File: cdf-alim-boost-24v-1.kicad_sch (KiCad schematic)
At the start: 0 parts

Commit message: schem: add batt input
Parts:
- added C2: 1u, Capacitor_SMD:C_0402_1005Metric, symbol Device:C
- added C3: 1n, Capacitor_SMD:C_0402_1005Metric, symbol Device:C
- added C7, C9: 10u, Capacitor_SMD:C_0805_2012Metric, symbol Device:C
- added D2: SMBJ6.0CA, Diode_SMD:D_SMA, symbol Device:D_TVS
- added D4: GREEN, LED_SMD:LED_0805_2012Metric, symbol Device:LED
- added J2: Conn_01x02, Connector_JST:JST_XH_S2B-XH-A-1_1x02_P2.50mm_Horizontal, symbol Connector_Generic:Conn_01x02
- added JP1: Jumper_2_Small_Bridged, Connector_PinHeader_2.54mm:PinHeader_1x02_P2.54mm_Vertical, symbol Jumper:Jumper_2_Small_Bridged
- added R11: 5k1, Resistor_SMD:R_0402_1005Metric, symbol Device:R
- added R5: 10k, Resistor_SMD:R_0402_1005Metric, symbol Device:R
- added R6: 1k, Resistor_SMD:R_0402_1005Metric, symbol Device:R
- added R7: 3k3, Resistor_SMD:R_0402_1005Metric, symbol Device:R
- added TP2: TestPoint, TestPoint:TestPoint_Pad_D2.0mm, symbol Connector:TestPoint
- added U1: TPS259470x, GLCS:Texas_RPW0010A_VQFN-HR-10_2x2mm_P0.5mm, symbol GLCS:TPS259470x
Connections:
- new net: C3.1, U1.7 (DVDT)
- new net: C2.2, D2.1 (A1), J2.2 (Pin_2), R5.2, U1.5 (IN)
- new net: D4.1 (K), U1.4 (~{FLT})
- new net: D4.2 (A), R11.1
- new net: JP1.1 (A), U1.6 (OUT)
- new net: C7.1, C9.1, JP1.2 (B)
- new net +3V3: R11.2
- new net BATT1_V: R5.1, R6.2, U1.1 (EN/UVLO)
- new net GND: C2.1, C3.2, C7.2, C9.2, D2.2 (A2), J2.1 (Pin_1), R6.1, R7.2, U1.2 (OVLO), U1.8 (GND)
- new net ILM1: R7.1, TP2.1, U1.9 (ILM)
- no-connect marks 0 -> 2
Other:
- note added: "UVLO = 13.2V Slew Rate 250mA limit for 100uF load -> 2.5V/ms -> Cdvdt = 800pF (BOM consolidation) For 1n -> SR ~ 2V/ms Ilim ->Ilim = 1A ->I = Vilm(µV)/(180*3300)"

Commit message: schem: remove efuse
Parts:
- removed C2: 1u, Capacitor_SMD:C_0402_1005Metric, symbol Device:C
- removed C3: 1n, Capacitor_SMD:C_0402_1005Metric, symbol Device:C
- removed C7, C9: 10u, Capacitor_SMD:C_0805_2012Metric, symbol Device:C
- removed D4: GREEN, LED_SMD:LED_0805_2012Metric, symbol Device:LED
- removed JP1: Jumper_2_Small_Bridged, Connector_PinHeader_2.54mm:PinHeader_1x02_P2.54mm_Vertical, symbol Jumper:Jumper_2_Small_Bridged
- removed R11: 5k1, Resistor_SMD:R_0402_1005Metric, symbol Device:R
- removed R5: 10k, Resistor_SMD:R_0402_1005Metric, symbol Device:R
- removed R6: 1k, Resistor_SMD:R_0402_1005Metric, symbol Device:R
- removed R7: 3k3, Resistor_SMD:R_0402_1005Metric, symbol Device:R
- removed TP2: TestPoint, TestPoint:TestPoint_Pad_D2.0mm, symbol Connector:TestPoint
- removed U1: TPS259470x, GLCS:Texas_RPW0010A_VQFN-HR-10_2x2mm_P0.5mm, symbol GLCS:TPS259470x
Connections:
- no-connect marks 2 -> 0
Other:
- note removed: "UVLO = 13.2V Slew Rate 250mA limit for 100uF load -> 2.5V/ms -> Cdvdt = 800pF (BOM consolidation) For 1n -> SR ~ 2V/ms Ilim ->Ilim = 1A ->I = Vilm(µV)/(180*3300)"
- moved on the sheet: D2

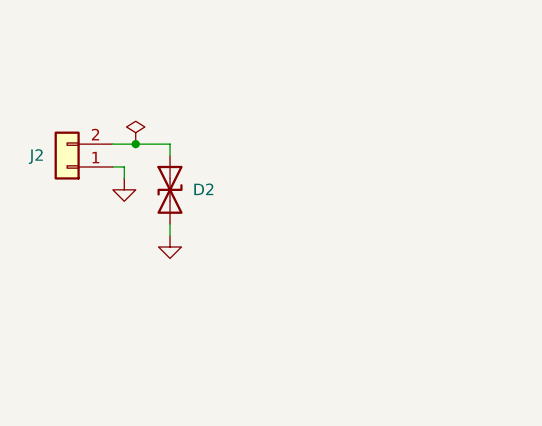
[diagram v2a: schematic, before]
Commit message: schem: add mosfet
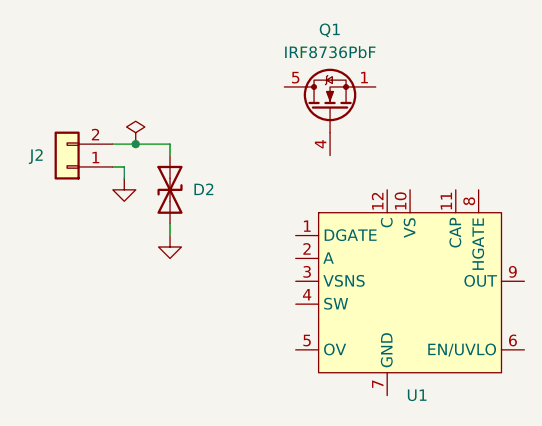
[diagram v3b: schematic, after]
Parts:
- added Q1: IRF8736PbF, Package_SO:SOIC-8_3.9x4.9mm_P1.27mm, symbol Transistor_FET:IRF8721PBF-1
- added U1: (no value), GLCS:WSON-12-1EP_3x3mm_P0.5mm_EP1.3x2.5mm_ThermalVias, symbol GLCS:LM74800
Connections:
- new net: Q1.1 (S), Q1.2 (S), Q1.3 (S)
- new net: Q1.5 (D), Q1.6 (D), Q1.7 (D), Q1.8 (D)
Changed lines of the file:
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@@
+	)
+	(symbol
+		(lib_id "Transistor_FET:IRF8721PBF-1")
+		(at 55.88 22.86 90)
+		(unit 1)
+		(body_style 1)
+		(exclude_from_sim no)
+		(in_bom yes)
+		(on_board yes)
+		(in_pos_files yes)
+		(dnp no)
+		(fields_autoplaced yes)
+		(property "Reference" "Q1"
+			(at 55.88 13.97 90)
+			(show_name no)
+			(do_not_autoplace no)
+			(effects
+				(font
+					(size 1.27 1.27)
+				)
+			)
+		)
+		(property "Value" "IRF8736PbF"
+			(at 55.88 16.51 90)
+			(show_name no)
+			(do_not_autoplace no)
+			(effects
+				(font
+					(size 1.27 1.27)
+				)
+			)
+		)
+		(property "Footprint" "Package_SO:SOIC-8_3.9x4.9mm_P1.27mm"
+			(at 57.785 17.78 0)
+			(hide yes)
+			(show_name no)
+			(do_not_autoplace no)
+			(effects
+				(font
+					(size 1.27 1.27)
+					(italic yes)
+				)
+				(justify left)
+			)
+		)
+		(property "Datasheet" "http://www.irf.com/product-info/datasheets/data/irf8721pbf-1.pdf"
+			(at 59.69 17.78 0)
+			(hide yes)
+			(show_name no)
+			(do_not_autoplace no)
+			(effects
+				(font
+					(size 1.27 1.27)
+				)
+				(justify left)
+			)
+		)
+		(property "Description" "14A Id, 30V Vds, HEXFET N-Channel MOSFET, SO-8"
+			(at 55.88 22.86 0)
+			(hide yes)
+			(show_name no)
+			(do_not_autoplace no)
+			(effects
+				(font
+					(size 1.27 1.27)
+				)
+			)
+		)
+		(pin "8"
+		)
+		(pin "2"
+		)
+		(pin "4"
+		)
+		(pin "7"
+		)
+		(pin "1"
+		)
+		(pin "5"
+		)
+		(pin "3"
+		)
+		(pin "6"
+		)
+		(instances
+			(project "cdf-alim-boost-24v-1"
+				(path "/c1d68e1e-31aa-4338-bfd5-3714fe43b2c6"
+					(reference "Q1")
+					(unit 1)
+				)
+			)
+		)
 	)
 	(symbol
@@
 					(unit 1)
 				)
+			)
+		)
+	)
+	(symbol
+		(lib_id "GLCS:LM74800")
+		(at 62.23 43.18 0)
+		(unit 1)
+		(body_style 1)
+		(exclude_from_sim no)
+		(in_bom yes)
+		(on_board yes)
+		(in_pos_files yes)
+		(dnp no)
+		(fields_autoplaced yes)
+		(property "Reference" "U1"
+			(at 64.3733 54.61 0)
+			(show_name no)
+			(do_not_autoplace no)
+			(effects
+				(font
+					(size 1.27 1.27)
+				)
+				(justify left)
+			)
+		)
+		(property "Value" ""
+			(at 62.23 43.18 0)
+			(show_name no)
+			(do_not_autoplace no)
+			(effects
+				(font
+					(size 1.27 1.27)
+				)
+			)
+		)
+		(property "Footprint" "GLCS:WSON-12-1EP_3x3mm_P0.5mm_EP1.3x2.5mm_ThermalVias"
+			(at 62.23 43.18 0)
+			(hide yes)
+			(show_name no)
+			(do_not_autoplace no)
+			(effects
+				(font
+					(size 1.27 1.27)
+				)
+			)
+		)
+		(property "Datasheet" ""
+			(at 62.23 43.18 0)
+			(hide yes)
+			(show_name no)
+			(do_not_autoplace no)
+			(effects
+				(font
+					(size 1.27 1.27)
+				)
+			)
+		)
+		(property "Description" ""
+			(at 62.23 43.18 0)
+			(hide yes)
+			(show_name no)
+			(do_not_autoplace no)
+			(effects
+				(font
+					(size 1.27 1.27)
+				)
+			)
+		)
+		(pin "9"
+		)
+		(pin "11"
+		)
+		(pin "7"
+		)
+		(pin "2"
+		)
+		(pin "1"
+		)
+		(pin "10"
+		)
+		(pin "4"
+		)
+		(pin "12"
+		)
+		(pin "8"
+		)
+		(pin "3"
+		)
+		(pin "RTN"
+		)
+		(pin "6"
+		)
+		(pin "5"
+		)
+		(instances
+			(project "cdf-alim-boost-24v-1"
+				(path "/c1d68e1e-31aa-4338-bfd5-3714fe43b2c6"
+					(reference "U1")
+					(unit 1)
+				)

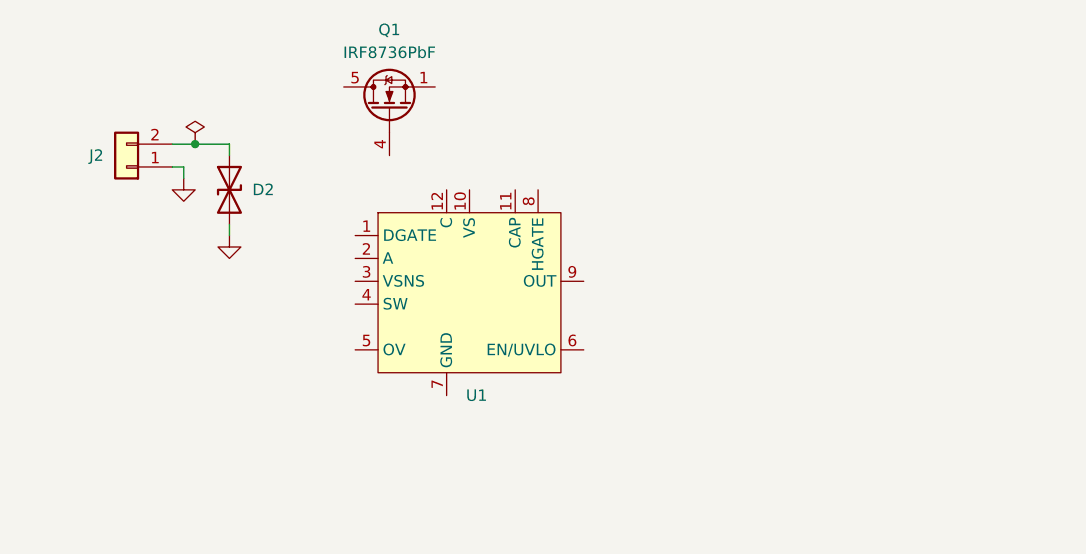
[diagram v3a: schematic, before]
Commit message: schem: initial ideal diode
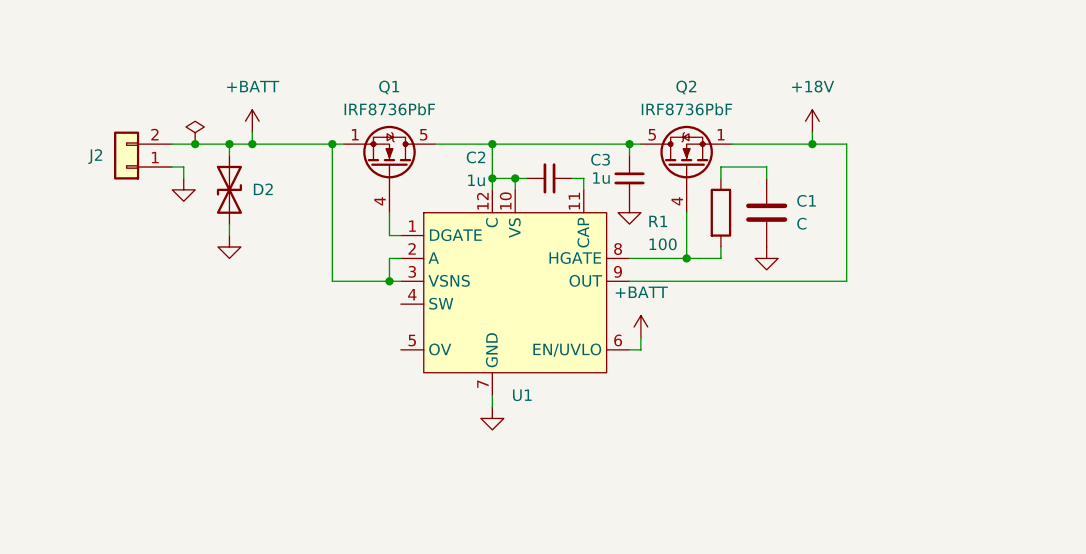
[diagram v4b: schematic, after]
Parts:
- added C1: C, symbol Device:C
- added C2, C3: 1u, Capacitor_SMD:C_0402_1005Metric, symbol Device:C_Small
- added Q2: IRF8736PbF, Package_SO:SOIC-8_3.9x4.9mm_P1.27mm, symbol Transistor_FET:IRF8721PBF-1
- added R1: 100, symbol Device:R
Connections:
- net GND: now also U1.7 (GND), C1.2, C3.1
- net +BATT: now reaches Q1.1 (S), Q1.2 (S), Q1.3 (S)
- net +BATT: now also D2.1 (A1), J2.2 (Pin_2), U1.2 (A), U1.3 (VSNS), U1.6 (EN/UVLO)
- net at Q1.4 (G): now also U1.1 (DGATE)
- net at Q1.5 (D), Q1.6 (D), Q1.7 (D)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: now also U1.10 (VS), U1.12 (C), C2.2, C3.2, Q2.5 (D), Q2.6 (D), Q2.7 (D), Q2.8 (D)
- net at U1.11 (CAP): now also C2.1
- net at U1.8 (HGATE): now also Q2.4 (G), R1.2
- net +18V: now reaches U1.9 (OUT)
- net +18V: now also Q2.1 (S), Q2.2 (S), Q2.3 (S)
- new net: C1.1, R1.1
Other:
- moved on the sheet: Q1, U1

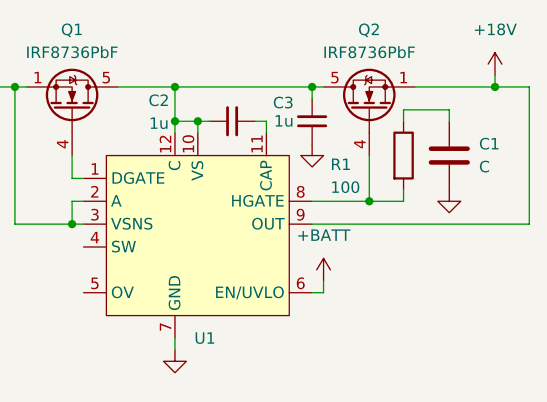
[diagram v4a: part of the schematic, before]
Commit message: schem: add ideal diode en connector
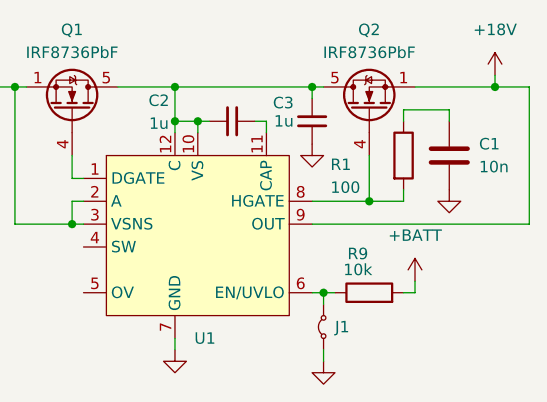
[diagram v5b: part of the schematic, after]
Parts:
- added J1: Conn_01x02, Connector_JST:JST_XH_S2B-XH-A-1_1x02_P2.50mm_Horizontal, symbol Jumper:Jumper_2_Small_Bridged
- added R9: 10k, Resistor_SMD:R_0402_1005Metric, symbol Device:R
- C1: value C -> 10n
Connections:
- net +BATT: now also R9.2; no longer U1.6 (EN/UVLO)
- net GND: now also J1.1 (A)
- new net: J1.2 (B), R9.1, U1.6 (EN/UVLO)

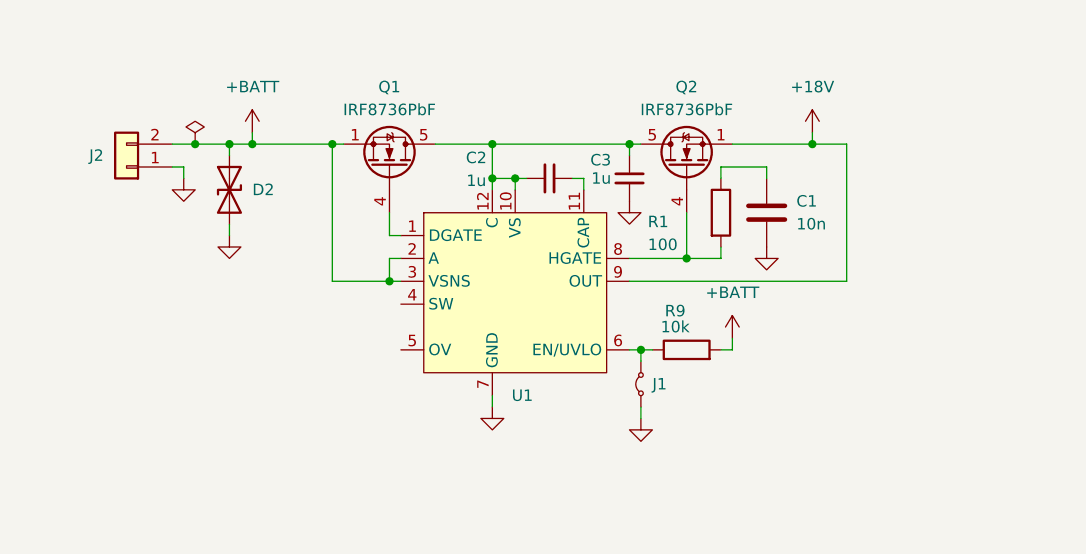
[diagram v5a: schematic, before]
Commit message: schem: finish lm7480 ideal diode
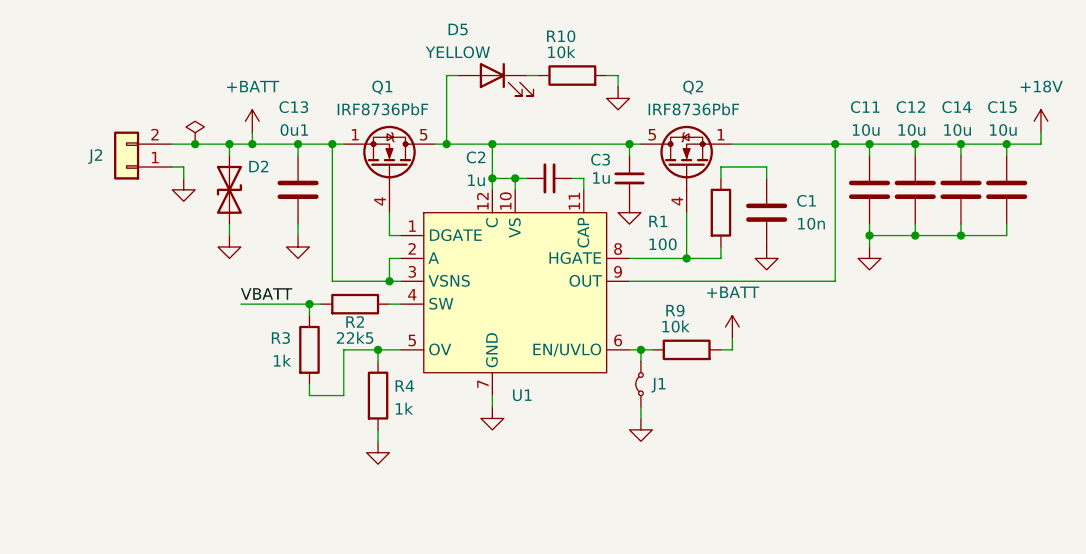
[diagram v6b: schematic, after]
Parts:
- added C11, C12, C14, C15: 10u, Capacitor_SMD:C_0805_2012Metric, symbol Device:C
- added C13: 0u1, Capacitor_SMD:C_0402_1005Metric, symbol Device:C
- added D5: YELLOW, LED_SMD:LED_0805_2012Metric, symbol Device:LED
- added R10: 10k, Resistor_SMD:R_0402_1005Metric, symbol Device:R
- added R2: 22k5, symbol Device:R
- added R3, R4: 1k, symbol Device:R
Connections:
- net +18V: now also C11.1, C12.1, C14.1, C15.1
- net +BATT: now also C13.1
- net GND: now also C11.2, C12.2, C13.2, C14.2, C15.2, R10.2, R4.2
- net at C2.2, C3.2, Q1.5 (D)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: now also D5.2 (A)
- net at U1.4 (SW): now also R2.1
- net at U1.5 (OV): now also R3.2, R4.1
- new net: D5.1 (K), R10.1
- new net VBATT: R2.2, R3.1

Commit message: schem: fix tvs value
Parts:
- D2: value SMBJ6.0CA -> SMAJ26CA
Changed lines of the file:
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@@
 			)
 		)
-		(property "Value" "SMBJ6.0CA"
+		(property "Value" "SMAJ26CA"
 			(at 40.64 33.0199 90)
 			(hide yes)

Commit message: schem: add text
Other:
- note added: "LM7480 +18V input protection"
- moved on the sheet: C1, C11, C12, C13, C14, C15, C2, C3, D2, D5, J1, J2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
